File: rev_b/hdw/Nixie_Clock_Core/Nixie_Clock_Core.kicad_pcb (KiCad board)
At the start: 6 copper layers, 200 x 50 mm, 329 parts, among them J1301 USB_B_Mini, J1901 Conn_02x32_Top_Bottom, J201 +24V IN, J202 +24V IN, J2101 I2C, J2102 USB UART, J801 PICKIT4, Q2101 BSS214NW, Q401 BSS214NW, Q402 ZXMS6004FFTA, Q601 IRFL214, Q701 BSS192PH6327FTSA1, Q801 BSS214NW, SW801 MRST, U1001 PIC32MZ2048EFG100_IPF, U1101 74LVC1G97, U1201 DS3231MZ, U1202 TLV6700, U1301 TLV6700, U1302 FT234XD, U1303 74LVC1G97, U1304 ISO7321C, U1305 TPD3S014DBVR, U1401 DS1683, U1501 74LVC1G97, U1502 74LVC1G97, U1503 74LVC1G97, U1504 74LVC1G97, U1505 74LVC1G97, U1601 74LVC1G97, U1602 74LVC1G97, U1603 74LVC1G97, U1604 74LVC1G97, U1701 74VHC541, U1702 74VHC541, U1703 74VHC541, U1801 TCA9803, U1802 74VHC541, U201 TPS26600RHFT, U2101 LTC6900, U2102 74LVC1G97, U2103 MCP9804, U301 INA219BxDCN, U302 MCP9804, U401 LT8609A-DD, U501 INA219BxDCN, U502 MCP9804, U601 TLV6700, U602 LT3757, U603 TLV6700, U701 OPA333xxDCK, U702 MCP9804, U703 INA219BxDCN, U704 OPA333xxDCK, U705 OPA333xxDCK, X1101 ASE-8.000MHz, X1102 ECS-327KE

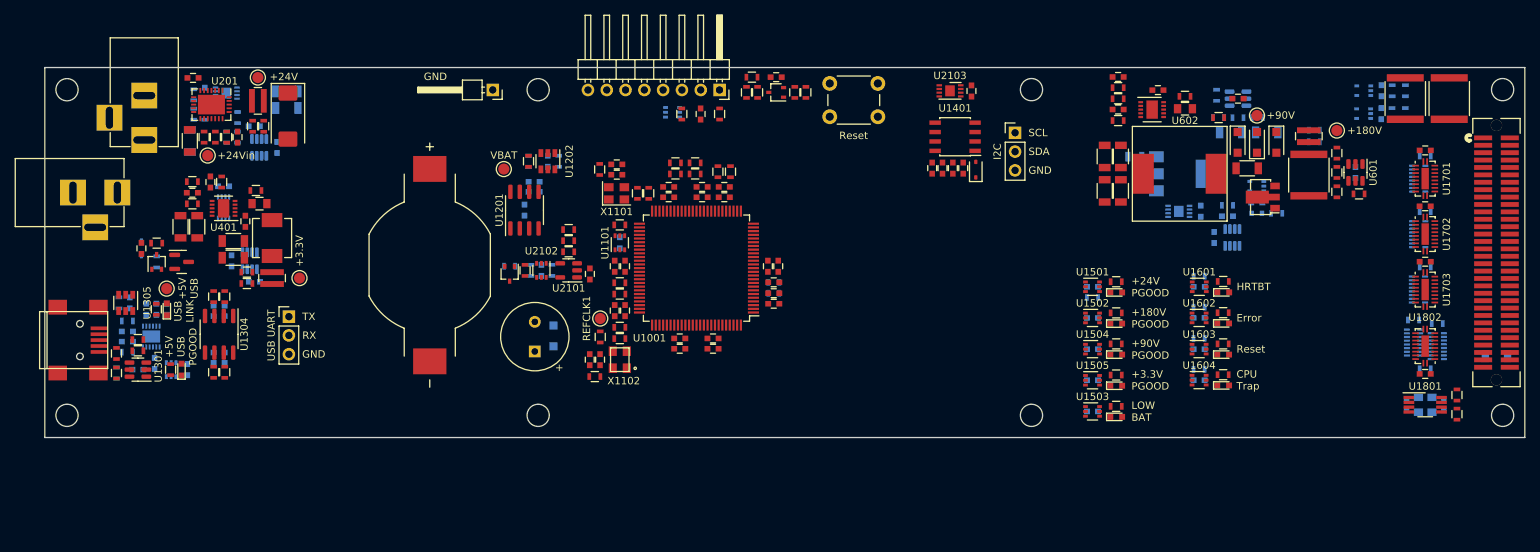
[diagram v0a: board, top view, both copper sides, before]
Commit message: started PCB design rules, some layout
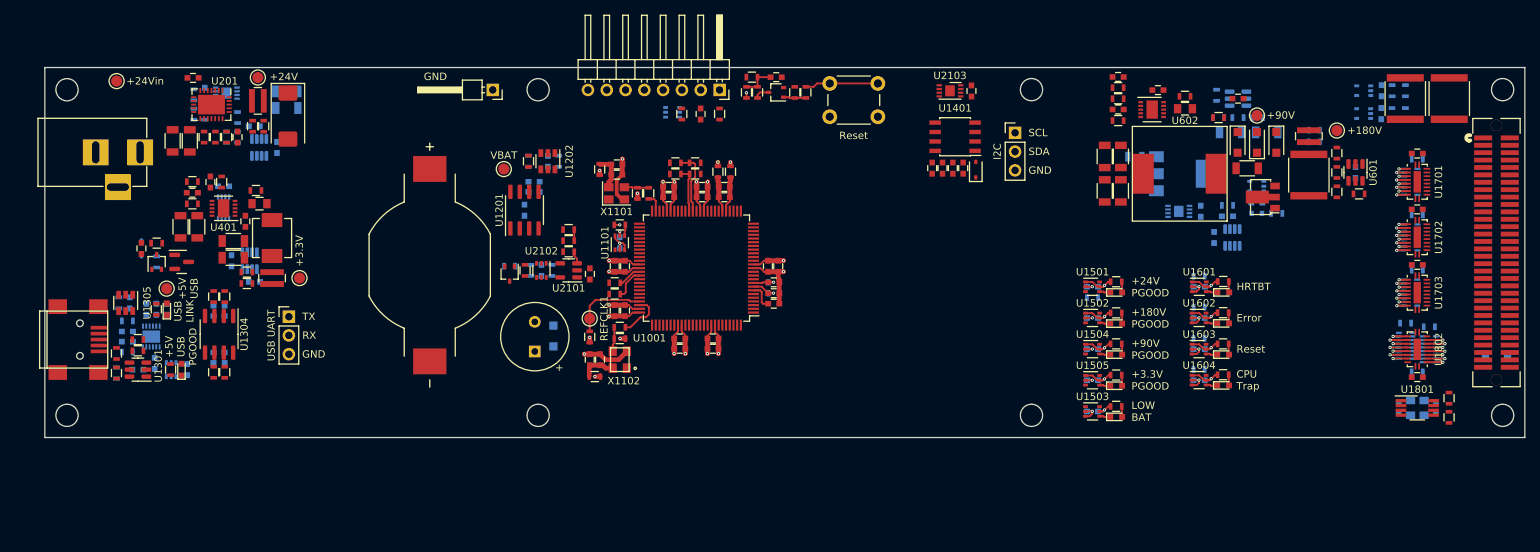
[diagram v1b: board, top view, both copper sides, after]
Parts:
- removed J202: +24V IN, Connectors:BARREL_JACK
- C202: moved to F.Cu
- moved TP202 15.9 mm to (44.7, 70.6)
- moved C202 2.32 mm to (52.3, 78.7)
- moved J201 1.76 mm to (47.9, 80.2), turned to 0 degrees
- moved R1101 1.42 mm to (108.7, 105.2)
- moved TP1101 1.42 mm to (108.7, 102.7)
- moved C1702 1.15 mm to (220.5, 87.9)
- moved C1703 1.15 mm to (220.5, 95.4)
- moved C1801 1.15 mm to (220.5, 110.6)
- moved R1801 1.15 mm to (218.9, 103.3)
- moved R1803 1.15 mm to (224.8, 116.0)
- moved R1805 1.15 mm to (224.8, 113.5)
- moved R1806 1.15 mm to (222.1, 103.8)
- moved RN1701 1.15 mm to (219.6, 84.2)
- moved RN1702 1.15 mm to (219.6, 91.7)
- moved RN1801 1.15 mm to (218.9, 106.4)
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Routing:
- net GND: track 0.00 -> 76.4 mm, vias 0 -> 24
- net +3.3V: track 0.00 -> 75.4 mm, vias 0 -> 21
- net PIC32MZ_REFCLK1: track 0.00 -> 10.6 mm
- net Net-(R801-Pad1): track 0.00 -> 9.92 mm
- net RTC_Hardstrap: track 0.00 -> 8.63 mm
- net ETC_Hardstrap: track 0.00 -> 6.30 mm
- net PIC32MZ_SOSC_EC: track 0.00 -> 6.27 mm
- net Net-(X1102-Vdd): track 0.00 -> 4.84 mm
- net GNDA_MZ: track 0.00 -> 4.83 mm
- net +3.3VA_MZ: track 0.00 -> 4.83 mm
- net Net-(X1101-Vdd): track 0.00 -> 4.81 mm
- net Net-(C801-Pad1): track 0.00 -> 4.59 mm
- net I2C_SCL: track 0.00 -> 4.33 mm
- net POS180_ADC: track 0.00 -> 3.82 mm, vias 0 -> 1
- net Pushbutton_4_DSP: track 0.00 -> 3.66 mm, vias 0 -> 1
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- added copper zone on In1.Cu, net GND
- added copper zone on In4.Cu, net GND
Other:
- board text added: "0"
- board text added: "0 mils"
- board text added: "0.02"
- board text added: "0.3937007874 mils"
- board text added: "0.5984251969 mils"
- board text added: "1"
- board text added: "1.377952756 mils"
- board text added: "15.7480315 mils"
- board text added: "3.8"
- board text added: "4.6"
- board text added: "7.984251969 mils"
- board text added: "8.283464567 mils"
- board text added: "B.Cu"
- board text added: "B.Mask"
- board text added: "B.Paste"
- board text added: "B.Silkscreen"
- board text added: "Bottom Silk Screen"
- board text added: "Bottom Solder Mask"
- board text added: "Bottom Solder Paste"
- board text added: "Color"
- board text added: "Dielectric 1"
- board text added: "Dielectric 2"
- board text added: "Dielectric 3"
- board text added: "Dielectric 4"
- board text added: "Dielectric 5"
- board text added: "Epsilon R"
- board text added: "F.Cu"
- board text added: "F.Mask"
- board text added: "F.Paste"
- board text added: "F.Silkscreen"
- board text added: "FR4"
- board text added: "In1.Cu"
- board text added: "In2.Cu"
- board text added: "In3.Cu"
- board text added: "In4.Cu"
- board text added: "JLC06161H-7628 Stackup"
- board text added: "Layer Name"
- board text added: "Loss Tangent"
- board text added: "Material"
- board text added: "Not specified"
- board text added: "Thickness (mils)"
- board text added: "Top Silk Screen"
- board text added: "Top Solder Mask"
- board text added: "Top Solder Paste"
- board text added: "Type"
- board text added: "copper"
- board text added: "core"
- board text added: "prepreg"

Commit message: lots of core board routing
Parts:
- added C709: 0.1uF, Capacitors_SMD:C_0603, B.Cu at (210.9, 71.9)
- added C710: 0.1uF, Capacitors_SMD:C_0603, B.Cu at (210.9, 75.0)
- C610: moved to B.Cu
- R1801: moved to F.Cu
- moved R617 6.37 mm to (211.1, 81.7), turned to 90 degrees
- moved R1801 5.48 mm to (217.5, 108.6), turned to 90 degrees
- moved TP601 5.31 mm to (210.2, 82.6)
- moved C605 5.28 mm to (212.6, 88.2)
- moved R601 5.28 mm to (210.1, 85.6)
- moved R602 5.28 mm to (210.1, 88.2)
- moved R603 5.28 mm to (210.1, 90.8)
- moved R605 5.28 mm to (213.1, 91.1)
- moved U601 5.28 mm to (212.6, 88.2)
- moved R1806 4.69 mm to (223.1, 108.4)
- moved R616 4.22 mm to (210.0, 78.5), turned to 0 degrees
- moved R615 3.80 mm to (209.0, 81.7), turned to 90 degrees
- moved C613 3.21 mm to (205.6, 80.1)
- moved TP602 2.65 mm to (200.2, 73.0)
- moved C610 2.42 mm to (196.3, 70.6)
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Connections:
- R1801 pad 2: Pushbutton_0 -> ~{Display_Detect}
- R1806 pad 2: Pushbutton_0_DSP -> ~{Display_Detect_DSP}
- RN1801 pad 16: unconnected-(RN1801-R1.2-Pad16) -> Pushbutton_0
- RN1801 pad 9: ~{Display_Detect} -> unconnected-(RN1801-R8.2-Pad9)
- RN1802 pad 16: ~{Display_Detect_DSP} -> unconnected-(RN1802-R1.2-Pad16)
- RN1802 pad 9: unconnected-(RN1802-R8.2-Pad9) -> Pushbutton_0_DSP
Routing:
- net GND: track 76.4 -> 167.6 mm, vias 24 -> 86
- net +3.3V: track 75.4 -> 128.4 mm, vias 21 -> 35
- net PIC32MZ_ICSPCLK: track 0.00 -> 36.0 mm
- net PIC32MZ_ICSPDAT: track 0.00 -> 27.1 mm
- net I2C_DSP_SDA: track 0.00 -> 20.9 mm, vias 0 -> 2
- net I2C_DSP_SCL: track 0.00 -> 16.7 mm
- net Cathode_9_DSP: track 0.00 -> 15.2 mm, vias 0 -> 2
- net Colon_1_DSP: track 0.00 -> 14.7 mm, vias 0 -> 2
- net Colon_3_DSP: track 0.00 -> 14.7 mm, vias 0 -> 2
- net Net-(Q601-G): track 0.00 -> 13.6 mm, vias 0 -> 1
- net Pushbutton_1_DSP: track 3.10 -> 16.7 mm, vias 1 -> 2
- net Pushbutton_3_DSP: track 3.09 -> 16.5 mm, vias 1 -> 2
- net Cathode_7_DSP: track 0.00 -> 13.4 mm, vias 0 -> 2
- net Pushbutton_5_DSP: track 3.10 -> 16.0 mm, vias 1 -> 2
- net Cathode_5_DSP: track 0.00 -> 12.3 mm, vias 0 -> 2
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- added copper zone on B.Cu, net +90V
- added copper zone on F.Cu, net +90V
- added copper zone on F.Cu, net Net-(C407-Pad1)
- added copper zone on B.Cu, net Net-(D601-A)
- added copper zone on F.Cu, net Net-(D601-A)
- added copper zone on F.Cu, net Net-(D602-K)
- added copper zone on F.Cu, net Net-(D603-K)
- added copper zone on B.Cu, net Net-(Q601-S)
- added copper zone on F.Cu, net Net-(U401-SW)

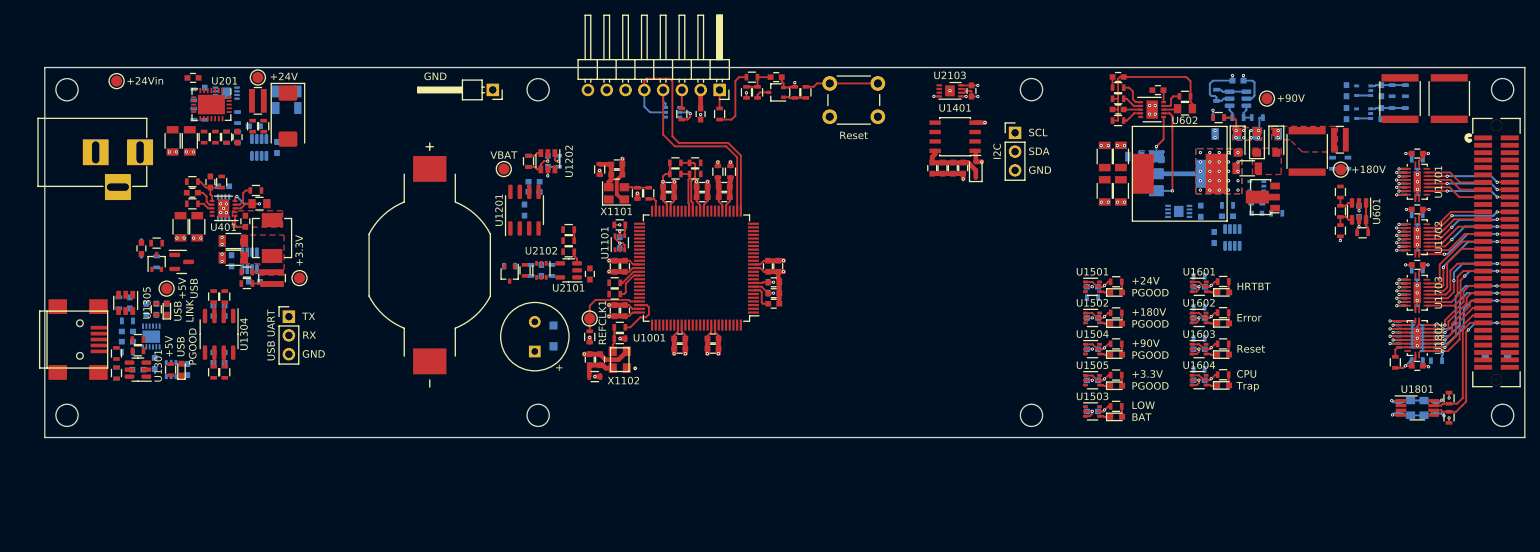
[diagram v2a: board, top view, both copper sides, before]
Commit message: lots more core board routing
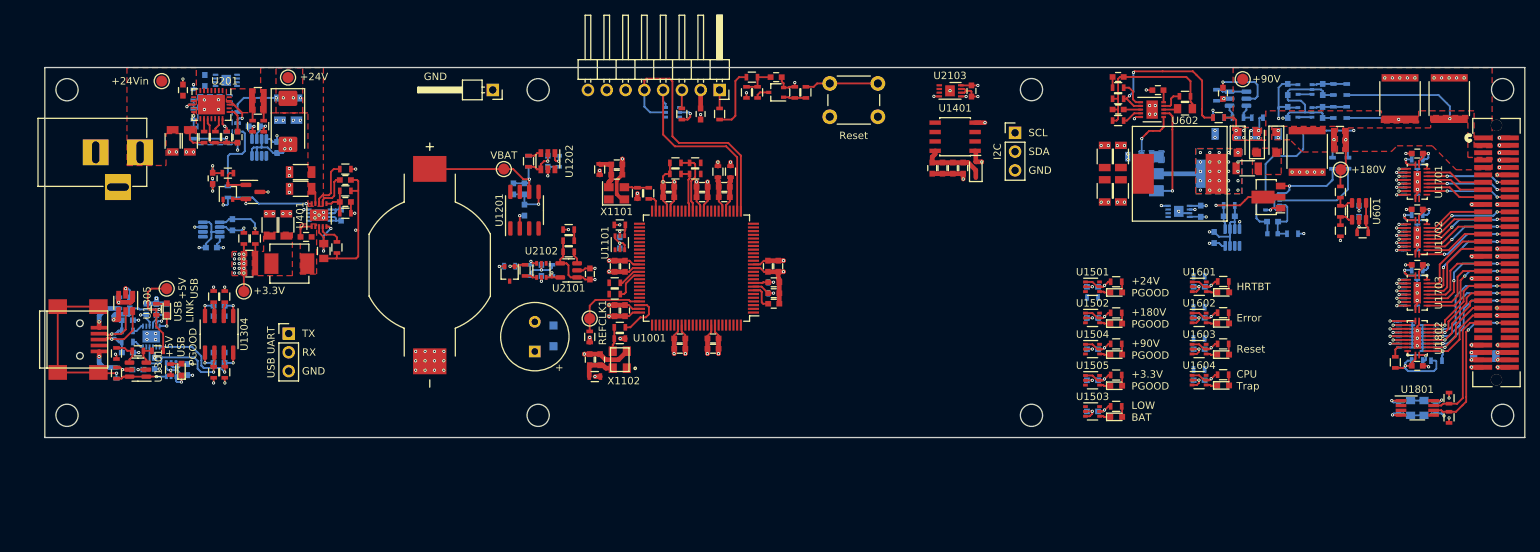
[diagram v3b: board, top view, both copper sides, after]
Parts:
- C610: moved to F.Cu
- moved R402 21.2 mm to (75.6, 82.5), turned to 180 degrees
- moved C404 20.7 mm to (75.6, 84.0), turned to 0 degrees
- moved R409 20.7 mm to (75.6, 85.4), turned to 0 degrees
- moved C409 18.4 mm to (75.6, 86.9), turned to 180 degrees
- moved C401 17.8 mm to (69.6, 82.9), turned to 180 degrees
- moved R408 17.2 mm to (75.6, 88.5), turned to 180 degrees
- moved C503 16.4 mm to (75.1, 88.7), turned to 90 degrees
- moved C403 14.9 mm to (69.6, 85.2), turned to 180 degrees
- moved C405 13.5 mm to (57.7, 83.8)
- moved D401 13.5 mm to (57.7, 83.8)
- moved Q401 13.5 mm to (59.8, 85.6)
- moved Q402 13.5 mm to (63.1, 85.6)
- moved R401 13.5 mm to (59.8, 85.6)
- moved R404 13.5 mm to (59.8, 83.0)
- moved R403 13.4 mm to (74.5, 93.1), turned to -90 degrees
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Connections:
- J1901 pad 1: +180V -> +90V
- J1901 pad 2: +180V -> +90V
- J1901 pad 4: +90V -> +180V
- J1901 pad 5: +90V -> +180V
- J1901 pad 6: GND -> unconnected-(J1901-Pin_6-Pad6)
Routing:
- net GND: track 167.6 -> 301.1 mm, vias 86 -> 163
- net +3.3V: track 128.4 -> 190.3 mm, vias 35 -> 72
- net +180V: track 0.00 -> 52.1 mm, vias 0 -> 3
- net +5V_USB: track 0.00 -> 26.3 mm, vias 0 -> 2
- net ~{IO_Level_Shift_Enable}: track 0.00 -> 25.7 mm, vias 0 -> 8
- net GND_USB: track 0.00 -> 24.3 mm, vias 0 -> 15
- net Net-(J1301-Shield): track 0.00 -> 23.1 mm, vias 0 -> 1
- net Net-(U602-FBX): track 2.70 -> 22.8 mm, vias 0 -> 2
- net VBAT: track 0.00 -> 20.1 mm, vias 0 -> 1
- net +3.3V_USB: track 0.00 -> 19.0 mm, vias 0 -> 8
- net POS24_PGOOD: track 0.00 -> 15.4 mm, vias 0 -> 1
- net POS180_SNS+: track 0.00 -> 14.1 mm, vias 0 -> 1
- net POS3P3_RUN: track 0.00 -> 14.0 mm, vias 0 -> 2
- net USB_UART_TX_ISO: track 1.95 -> 15.5 mm, vias 0 -> 1
- net Net-(Q701-D): track 0.00 -> 13.4 mm, vias 0 -> 1
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- added copper zone on F.Cu, net +180V
- added copper zone on F.Cu, net +24V
- added copper zone on F.Cu, net +24Vin
- added copper zone on F.Cu, net +3.3V
- added copper zone on In2.Cu, net +3.3V
- added copper zone on In2.Cu, net +3.3V_USB
- added copper zone on In1.Cu, net GND_USB
- added copper zone on In4.Cu, net GND_USB
- added copper zone on F.Cu, net Net-(R205-Pad2)
- added copper zone on B.Cu, net Net-(U201-RTN)

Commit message: lots of core board routing
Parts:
- moved R611 2.99 mm to (184.3, 78.5)
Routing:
- net ~{PIC32MZ_MCLR}: track 8.76 -> 32.5 mm
- net PGOOD_LED_SHDN: track 0.00 -> 21.9 mm, vias 0 -> 1
- net GND: track 301.1 -> 320.0 mm, vias 163 -> 175
- net +24V: track 13.2 -> 25.4 mm, vias 4 -> 64
- net Net-(BZ2101-+): track 0.00 -> 11.0 mm
- net +3.3V: track 190.3 -> 201.0 mm, vias 72 -> 75
- net Net-(Q601-S): track 7.44 -> 3.80 mm
- net Error_LED: track 0.00 -> 1.67 mm, vias 0 -> 1
- net CPU_Trap_LED: track 0.00 -> 1.52 mm, vias 0 -> 1
- net Heartbeat_LED: track 0.00 -> 1.45 mm, vias 0 -> 1
- net Reset_LED: track 0.00 -> 1.38 mm, vias 0 -> 1
- net ~{Display_Detect}: track 2.77 -> 3.34 mm, vias 0 -> 1
- added copper zone on B.Cu, net +24V

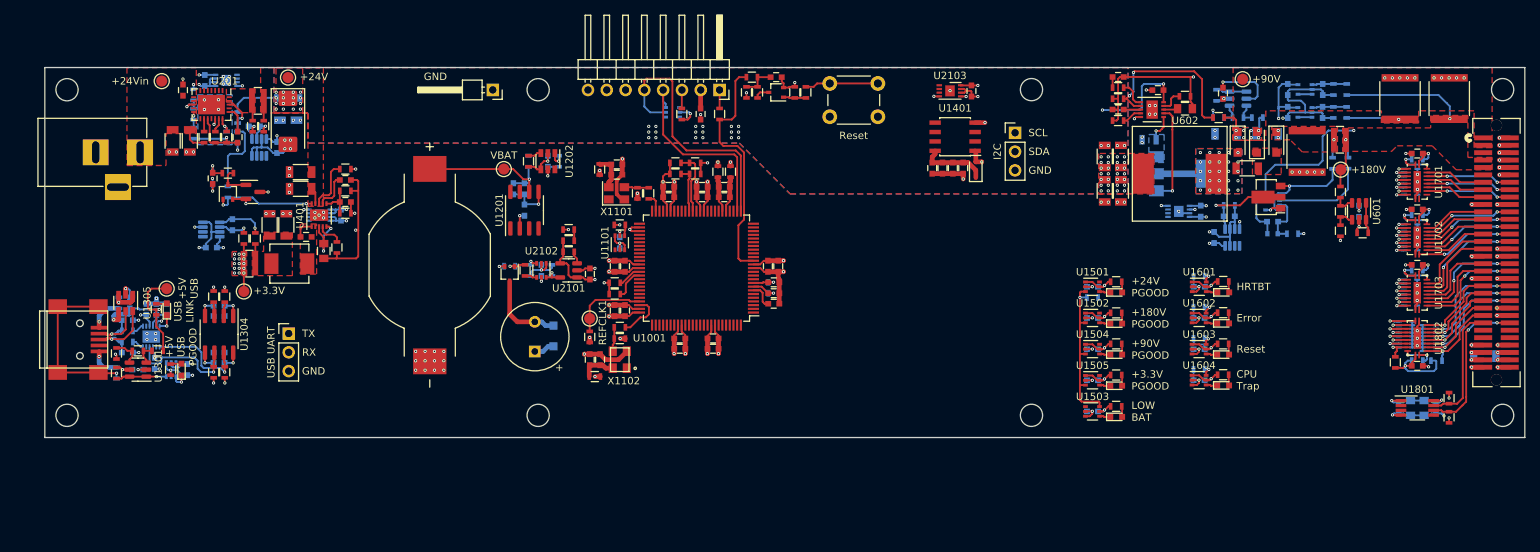
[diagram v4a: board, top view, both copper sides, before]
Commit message: routed all IO signals from buffers to PIC
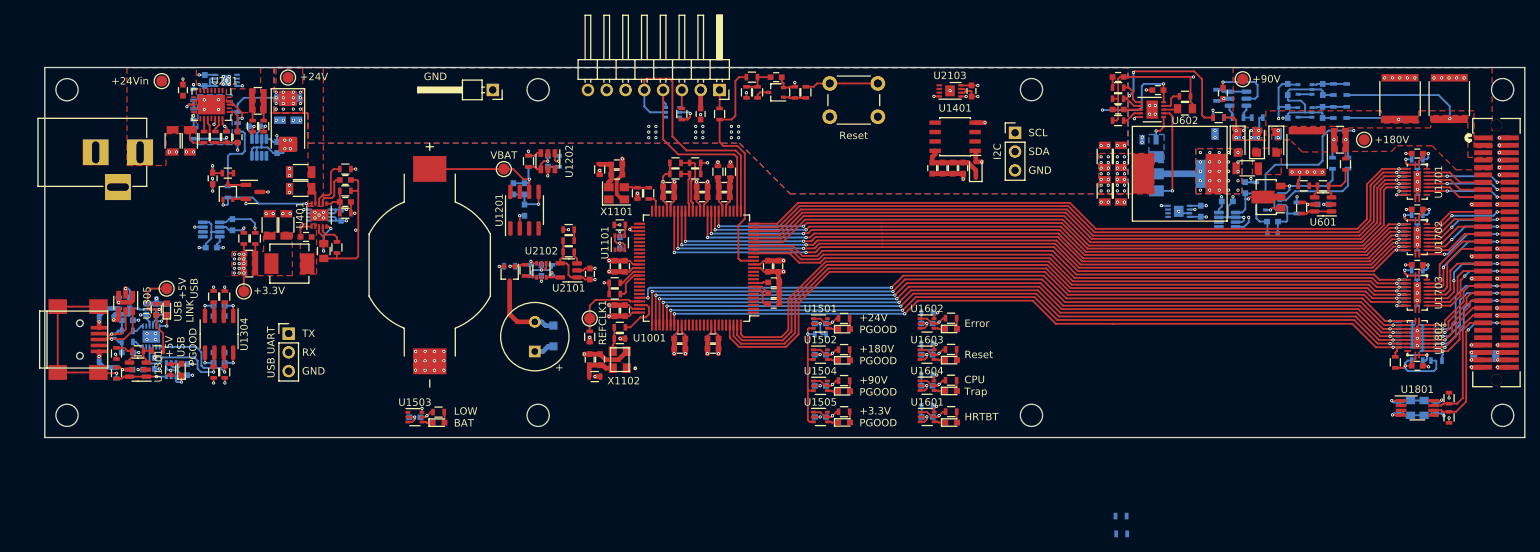
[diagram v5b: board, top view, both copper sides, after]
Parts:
- moved C1503 91.6 mm to (85.0, 116.0)
- moved D1503 91.6 mm to (88.2, 116.8)
- moved R1504 91.6 mm to (88.2, 115.3)
- moved U1503 91.6 mm to (85.0, 116.0)
- moved R708 58.0 mm to (180.5, 131.8)
- moved R707 55.8 mm to (180.5, 129.4)
- moved C1601 40.8 mm to (154.3, 116.0)
- moved D1601 40.8 mm to (157.5, 116.7)
- moved R1601 40.8 mm to (154.3, 114.6)
- moved U1601 40.8 mm to (154.3, 116.0)
- moved R1603 40.8 mm to (157.5, 115.3)
- moved C1501 37.1 mm to (139.8, 103.4)
- moved C1502 37.1 mm to (139.8, 107.6)
- moved C1504 37.1 mm to (139.8, 111.8)
- moved C1505 37.1 mm to (139.8, 116.0)
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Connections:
- U1001 pad 100: Anode_4 -> Colon_0
- U1001 pad 17: unconnected-(U1001-RA0/TMS/EBIA16/AN24-Pad17) -> Cathode_DP
- U1001 pad 18: Heartbeat_LED -> Cathode_9
- U1001 pad 19: CPU_Trap_LED -> Cathode_8
- U1001 pad 20: PGOOD_LED_SHDN -> Anode_5
- U1001 pad 21: Buzzer_Enable -> Anode_4
- U1001 pad 22: Colon_3 -> Anode_3
- U1001 pad 23: Colon_2 -> Anode_2
- U1001 pad 24: Colon_1 -> Anode_1
- U1001 pad 25: Colon_0 -> Anode_0
- U1001 pad 3: Anode_5 -> unconnected-(U1001-RE5/EBID5/AN17/RPE5/PMD5-Pad3)
- U1001 pad 32: Pushbutton_0 -> Cathode_0
- U1001 pad 33: Pushbutton_1 -> Cathode_1
- U1001 pad 34: Pushbutton_2 -> Cathode_2
- U1001 pad 35: Pushbutton_3 -> Cathode_3
- U1001 pad 41: Pushbutton_4 -> Cathode_4
- U1001 pad 42: Pushbutton_5 -> Cathode_5
- U1001 pad 43: Pushbutton_6 -> Cathode_6
- U1001 pad 44: ~{Display_Detect} -> Cathode_7
- U1001 pad 68: Cathode_6 -> unconnected-(U1001-RD9/EBIA15/RPD9/PMCS2/PMA15-Pad68)
- U1001 pad 69: Cathode_7 -> unconnected-(U1001-RD10/RPD10/SCK4-Pad69)
- U1001 pad 70: Cathode_8 -> unconnected-(U1001-RD11/EMDC/AEMDC/RPD11-Pad70)
- U1001 pad 71: Cathode_0 -> Pushbutton_0
- U1001 pad 76: Cathode_1 -> Pushbutton_1
- U1001 pad 77: Cathode_2 -> Pushbutton_2
- U1001 pad 78: Cathode_3 -> Pushbutton_3
- U1001 pad 79: Cathode_9 -> Pushbutton_4
- U1001 pad 80: Cathode_DP -> Pushbutton_5
- U1001 pad 81: Cathode_4 -> Pushbutton_6
- U1001 pad 82: Cathode_5 -> ~{Display_Detect}
- U1001 pad 91: Anode_0 -> unconnected-(U1001-RE0/EBID0/PMD0-Pad91)
- U1001 pad 94: Anode_1 -> unconnected-(U1001-RE1/EBID1/PMD1-Pad94)
- U1001 pad 97: unconnected-(U1001-RG13/TRD0/SQID0-Pad97) -> Colon_3
- U1001 pad 98: Anode_2 -> Colon_2
- U1001 pad 99: Anode_3 -> Colon_1
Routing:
- net Pushbutton_1: track 2.78 -> 110.7 mm, vias 1 -> 3
- net Pushbutton_2: track 3.59 -> 110.1 mm, vias 1 -> 3
- net Cathode_7: track 2.43 -> 108.5 mm, vias 1 -> 3
- net Pushbutton_3: track 2.78 -> 108.7 mm, vias 1 -> 3
- net Pushbutton_0: track 4.66 -> 110.5 mm, vias 1 -> 3
- net Cathode_6: track 1.81 -> 107.1 mm, vias 1 -> 3
- net Pushbutton_4: track 3.59 -> 108.1 mm, vias 1 -> 3
- net Pushbutton_5: track 2.78 -> 106.8 mm, vias 1 -> 3
- net Cathode_5: track 2.42 -> 106.4 mm, vias 1 -> 3
- net Cathode_4: track 1.82 -> 105.2 mm, vias 1 -> 3
- net Pushbutton_6: track 3.59 -> 106.2 mm, vias 1 -> 3
- net ~{Display_Detect}: track 3.34 -> 105.5 mm, vias 1 -> 3
- net Colon_3: track 1.81 -> 102.8 mm
- net Colon_2: track 2.42 -> 102.3 mm
- net Cathode_3: track 2.42 -> 102.0 mm, vias 1 -> 3
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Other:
- board text added: "TO-DO: * PIC32MZ Logo * Owl * Layer legend * COM port settings * Project title * Project rev * Project date * Layout stats * Coin Cell Name * PICK KIT 4 Logo * Center positive logo * High voltage warnings * Easter egg under PIC"
